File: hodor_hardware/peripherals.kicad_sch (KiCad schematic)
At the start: 59 parts, among them J2 Screw_Terminal_01x05, J3 Screw_Terminal_01x03, J5 Screw_Terminal_01x03, K1 FINDER-32.21-x000, K2 FINDER-32.21-x000, Q2 FDG1024NZ, Q3 FDG1024NZ, Q4 FDG1024NZ, Q6 BSS138DW, T4 IN2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

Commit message: Schematic finished
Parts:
- removed Q4: FDG1024NZ, Package_TO_SOT_SMD:SOT-363_SC-70-6, symbol Transistor_FET:FDG1024NZ
- added D25, D31: PMEG6010, Diode_SMD:D_SOD-128, symbol Device:D_Schottky
- added D32, D33: BCX84C15V, Diode_SMD:D_SOD-523, symbol Device:D_Zener
- added F2, F3: 1A, Diode_SMD:D_1812_4532Metric, symbol Device:Polyfuse_Small
- added J10: Screw_Terminal_01x03, TerminalBlock_Phoenix:TerminalBlock_Phoenix_PT-1,5-3-3.5-H_1x03_P3.50mm_Horizontal, symbol Connector:Screw_Terminal_01x03
- added Q10: BC847BDW1, Package_TO_SOT_SMD:SOT-363_SC-70-6, symbol Transistor_BJT:BC847BDW1
- added unit 1 of Q3
- added Q9: DMP6050SSD, Package_SO:SOIC-8_3.9x4.9mm_P1.27mm, symbol Transistor_FET:DMP6050SSD
- added R78, R80, R83, R84: 10k, Resistor_SMD:R_0402_1005Metric, symbol Device:R
- added R79, R82: 1k, Resistor_SMD:R_0402_1005Metric, symbol Device:R
- added R81, R85: 2.2k, Resistor_SMD:R_0402_1005Metric, symbol Device:R
- C3, C4, C5, C6, C7, C8: value 100n -> 100nF
- J2: footprint (none) -> TerminalBlock_Phoenix:TerminalBlock_Phoenix_PT-1,5-5-3.5-H_1x05_P3.50mm_Horizontal
- J3, J5: footprint (none) -> TerminalBlock_Phoenix:TerminalBlock_Phoenix_PT-1,5-3-3.5-H_1x03_P3.50mm_Horizontal
- T4, T5, T7, T8: now left out of the parts list
- U3, U4: footprint (none) -> Package_TO_SOT_SMD:SOT-23-6
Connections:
- net GND: now also D25.2 (A), D31.2 (A), J10.1 (Pin_1), Q10.1 (E1), Q10.4 (E2), Q3.1 (S), R80.1, R83.1
- net at D12.2 (A), R9.2: now also Q3.6 (D); no longer Q3.3 (D)
- net at D15.2 (A), R11.2: now also Q3.3 (D)
- net at R10.1, R18.1: now also Q3.5 (G)
- net at R16.1, R8.1: now also Q3.2 (G); no longer Q3.5 (G)
- new net: F3.1, Q9.5 (D2), Q9.6 (D2)
- new net: D31.1 (K), F3.2, J10.2 (Pin_2)
- new net: D25.1 (K), F2.2, J10.3 (Pin_3)
- new net: Q10.2 (B1), R79.2, R80.2
- new net: Q10.6 (C1), R81.2
- new net: D32.2 (A), Q9.2 (G1), R78.2, R81.1
- new net: Q10.3 (C2), R85.2
- new net: Q10.5 (B2), R82.2, R83.2
- new net: F2.1, Q9.7 (D1), Q9.8 (D1)
- new net: D33.2 (A), Q9.4 (G2), R84.2, R85.1
- new net OUT_CTRL_1: R79.1
- new net OUT_CTRL_2: R82.1
- new net V_{DC}: D32.1 (K), D33.1 (K), Q9.1 (S1), Q9.3 (S2), R78.1, R84.1
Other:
- note added: "2 switchable V_{DC} outputs with freewheeling diode and fuse"
- moved on the sheet: C5, C6, C7, D10, D11, D12, D13, D14, D15, D26, D27, D7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

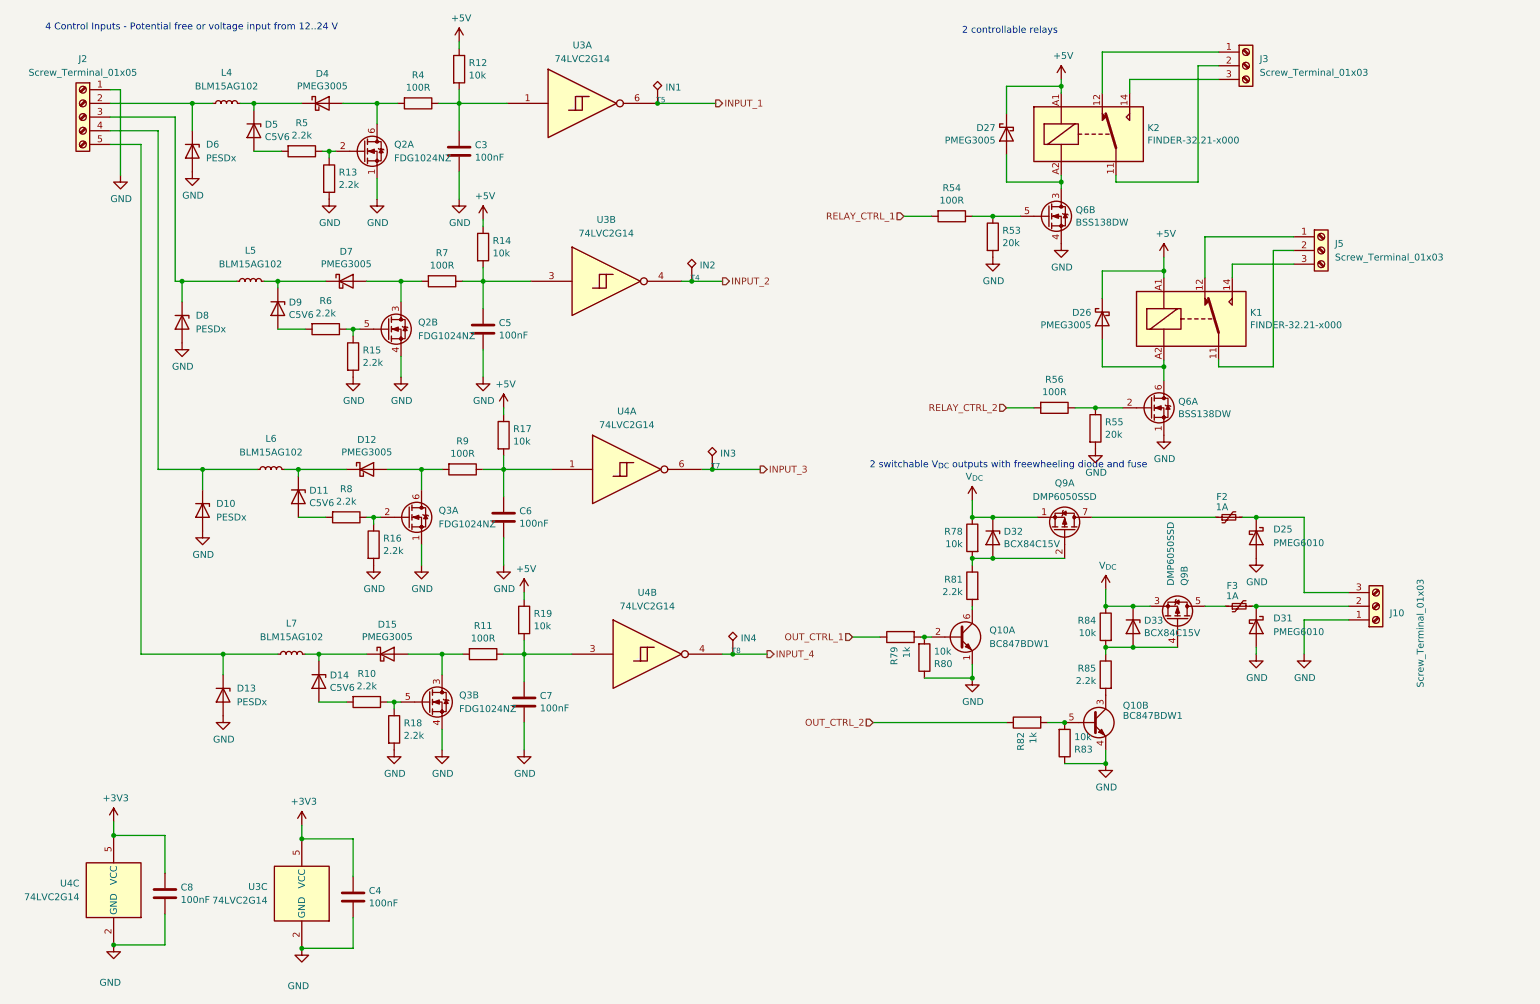
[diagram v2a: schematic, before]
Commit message: Reworked into 2 PCBs
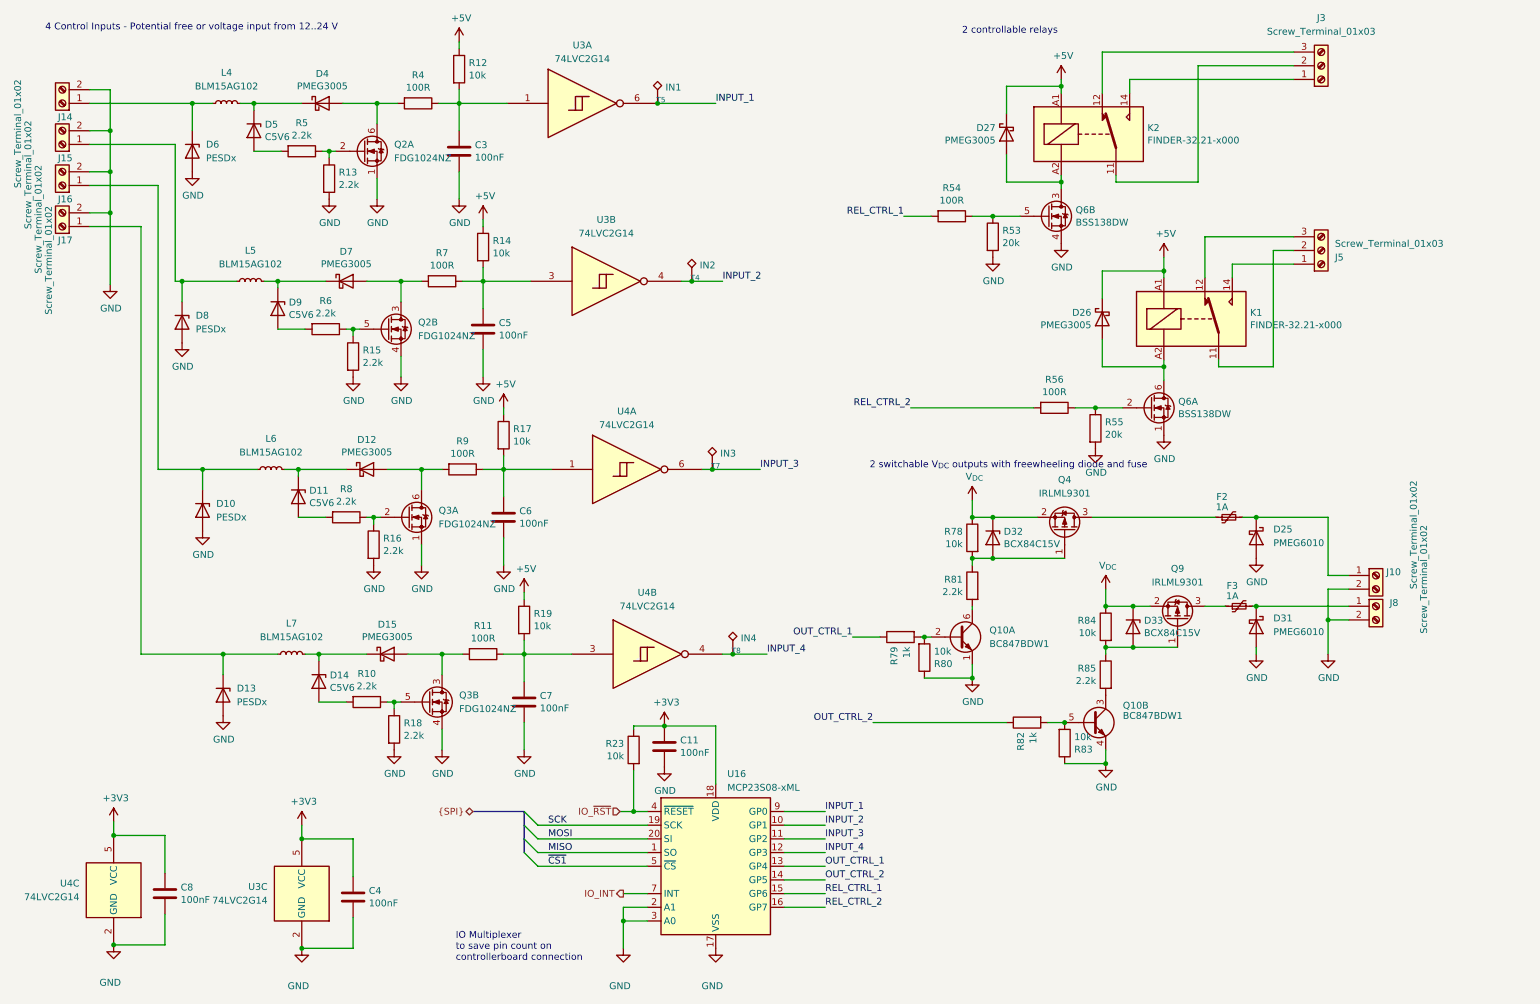
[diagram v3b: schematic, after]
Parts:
- removed J10: Screw_Terminal_01x03, TerminalBlock_Phoenix:TerminalBlock_Phoenix_PT-1,5-3-3.5-H_1x03_P3.50mm_Horizontal, symbol Connector:Screw_Terminal_01x03
- removed J2: Screw_Terminal_01x05, TerminalBlock_Phoenix:TerminalBlock_Phoenix_PT-1,5-5-3.5-H_1x05_P3.50mm_Horizontal, symbol Connector:Screw_Terminal_01x05
- removed Q9: DMP6050SSD, Package_SO:SOIC-8_3.9x4.9mm_P1.27mm, symbol Transistor_FET:DMP6050SSD
- added C11: 100nF, Capacitor_SMD:C_0402_1005Metric, symbol Device:C
- added J10, J14, J15, J16, J17, J8: Screw_Terminal_01x02, TerminalBlock_Phoenix:TerminalBlock_Phoenix_PT-1,5-2-3.5-H_1x02_P3.50mm_Horizontal, symbol Connector:Screw_Terminal_01x02
- added Q4, Q9: IRLML9301, Package_TO_SOT_SMD:SOT-23, symbol Transistor_FET:IRLML9301
- added R23: 10k, Resistor_SMD:R_0402_1005Metric, symbol Device:R
- added U16: MCP23S08-xML, Package_DFN_QFN:QFN-20-1EP_4x4mm_P0.5mm_EP2.7x2.7mm, symbol hodor_custom_parts:MCP23S08-xML
- D10, D13, D6, D8: footprint Diode_SMD:D_SOD-523 -> Diode_SMD:Nexperia_DSN1608-2_1.6x0.8mm
- D25, D31: footprint Diode_SMD:D_SOD-128 -> Diode_SMD:D_SOD-123F
- F2, F3: footprint Diode_SMD:D_1812_4532Metric -> Fuse:Fuse_1210_3225Metric
- J3, J5: footprint TerminalBlock_Phoenix:TerminalBlock_Phoenix_PT-1,5-3-3.5-H_1x03_P3.50mm_Horizontal -> TerminalBlock_Phoenix:TerminalBlock_Phoenix_MKDS-1,5-3_1x03_P5.00mm_Horizontal
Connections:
- net +3V3: now also C11.1, R23.1, U16.18 (VDD)
- net GND: now also C11.2, J10.2 (Pin_2), J14.2 (Pin_2), J15.2 (Pin_2), J16.2 (Pin_2), J17.2 (Pin_2), J8.2 (Pin_2), U16.17 (VSS), U16.2 (A1), U16.3 (A0)
- net INPUT_1: now also U16.9 (GP0)
- net INPUT_2: now also U16.10 (GP1)
- net INPUT_3: now also U16.11 (GP2)
- net INPUT_4: now also U16.12 (GP3)
- net OUT_CTRL_1: now also U16.13 (GP4)
- net OUT_CTRL_2: now also U16.14 (GP5)
- net V_{DC}: now also Q4.2 (S), Q9.2 (S)
- net at K2.12: now also J3.3 (Pin_3); no longer J3.1 (Pin_1)
- net at K2.14: now also J3.1 (Pin_1); no longer J3.3 (Pin_3)
- net at K1.12: now also J5.3 (Pin_3); no longer J5.1 (Pin_1)
- net at K1.14: now also J5.1 (Pin_1); no longer J5.3 (Pin_3)
- net at F3.1: now also Q9.3 (D)
- net at D31.1 (K), F3.2: now also J8.1 (Pin_1)
- net at D6.1 (K), L4.1: now also J14.1 (Pin_1)
- net at D8.1 (K), L5.1: now also J15.1 (Pin_1)
- net at D10.1 (K), L6.1: now also J16.1 (Pin_1)
- net at D13.1 (K), L7.1: now also J17.1 (Pin_1)
- net at D25.1 (K), F2.2: now also J10.1 (Pin_1)
- net at D32.2 (A), R78.2, R81.1: now also Q4.1 (G)
- net at F2.1: now also Q4.3 (D)
- net at D33.2 (A), R84.2, R85.1: now also Q9.1 (G)
- net RELAY_CTRL_1 renamed REL_CTRL_1
- net REL_CTRL_1: now also U16.15 (GP6)
- net RELAY_CTRL_2 renamed REL_CTRL_2
- net REL_CTRL_2: now also U16.16 (GP7)
- new net IO_INT: U16.7 (INT)
- new net IO_~{RST}: R23.2, U16.4 (~{RESET})
- new net MISO: U16.1 (SO)
- new net MOSI: U16.20 (SI)
- new net SCK: U16.19 (SCK)
- new net ~{CS1}: U16.5 (~{CS})
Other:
- note added: "IO Multiplexer to save pin count on controllerboard connection"
- moved on the sheet: J3

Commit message: Finished schematic and initial placement on PCB
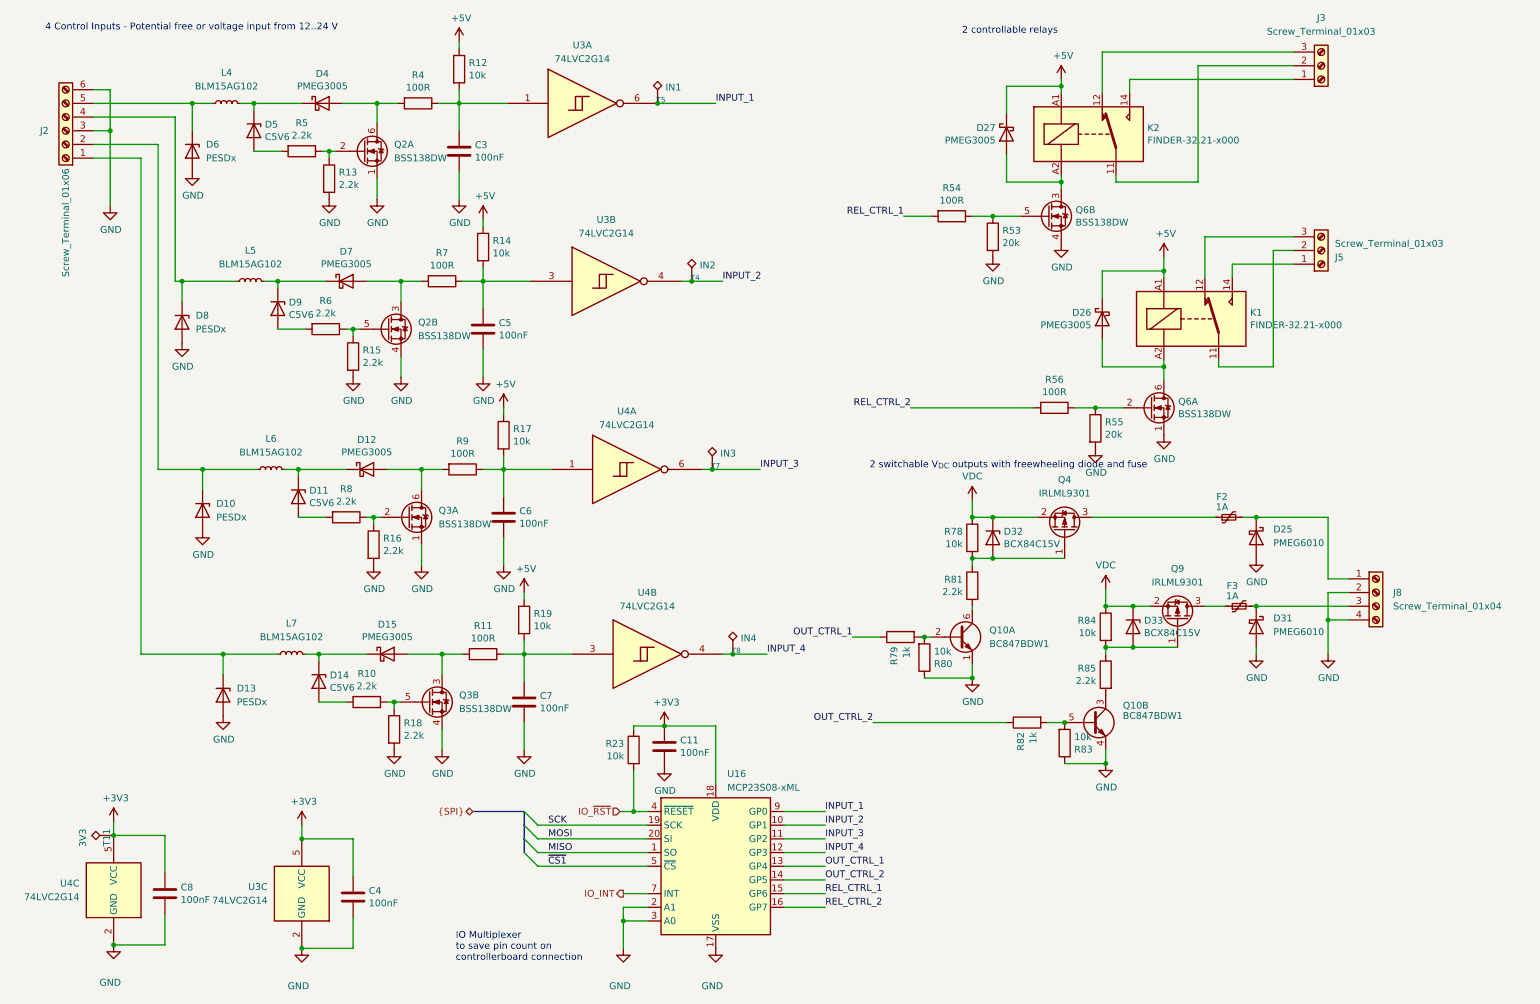
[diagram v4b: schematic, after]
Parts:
- removed J10, J14, J15, J16, J17, J8: Screw_Terminal_01x02, TerminalBlock_Phoenix:TerminalBlock_Phoenix_PT-1,5-2-3.5-H_1x02_P3.50mm_Horizontal, symbol Connector:Screw_Terminal_01x02
- added J2: Screw_Terminal_01x06, TerminalBlock_Phoenix:TerminalBlock_Phoenix_MKDS-1,5-6_1x06_P5.00mm_Horizontal, symbol Connector:Screw_Terminal_01x06
- added J8: Screw_Terminal_01x04, TerminalBlock_Phoenix:TerminalBlock_Phoenix_MKDS-1,5-4_1x04_P5.00mm_Horizontal, symbol Connector:Screw_Terminal_01x04
- added T11: 3V3, TestPoint:TestPoint_Pad_D1.0mm, symbol Connector:TestPoint_Alt
- Q2, Q3: value FDG1024NZ -> BSS138DW
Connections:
- net +3V3: now also T11.1
- net GND: now also J2.3 (Pin_3), J2.6 (Pin_6), J8.2 (Pin_2), J8.4 (Pin_4)
- net at D10.1 (K), L6.1: now also J2.2 (Pin_2)
- net at D31.1 (K), F3.2: now also J8.3 (Pin_3)
- net at D25.1 (K), F2.2: now also J8.1 (Pin_1)
- net at D8.1 (K), L5.1: now also J2.4 (Pin_4)
- net at D6.1 (K), L4.1: now also J2.5 (Pin_5)
- net at D13.1 (K), L7.1: now also J2.1 (Pin_1)
- net V_{DC} renamed VDC

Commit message: Initialized SW project
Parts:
- D10, D13, D6, D8: footprint Diode_SMD:Nexperia_DSN1608-2_1.6x0.8mm -> Diode_SMD:D_SOD-523
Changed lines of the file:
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@@
 			)
 		)
-		(property "Footprint" "Diode_SMD:Nexperia_DSN1608-2_1.6x0.8mm"
+		(property "Footprint" "Diode_SMD:D_SOD-523"
 			(at 41.91 41.275 0)
 			(effects
@@
 			)
 		)
-		(property "Footprint" "Diode_SMD:Nexperia_DSN1608-2_1.6x0.8mm"
+		(property "Footprint" "Diode_SMD:D_SOD-523"
 			(at 40.005 73.025 0)
 			(effects
@@
 			)
 		)
-		(property "Datasheet" "https://assets.nexperia.com/documents/data-sheet/PTVS26VZ1USK.pdf"
+		(property "Datasheet" ""
 			(at 44.45 73.025 0)
 			(effects
@@
 			)
 		)
-		(property "Description" "26V, 1850W TVS unidirectional diode, DSN1608-2"
+		(property "Description" ""
 			(at 44.45 73.025 0)
 			(effects
@@
 			)
 		)
-		(property "Footprint" "Diode_SMD:Nexperia_DSN1608-2_1.6x0.8mm"
+		(property "Footprint" "Diode_SMD:D_SOD-523"
 			(at 47.625 142.24 0)
 			(effects
@@
 			)
 		)
-		(property "Datasheet" "https://assets.nexperia.com/documents/data-sheet/PTVS26VZ1USK.pdf"
+		(property "Datasheet" ""
 			(at 52.07 142.24 0)
 			(effects
@@
 			)
 		)
-		(property "Description" "26V, 1850W TVS unidirectional diode, DSN1608-2"
+		(property "Description" ""
 			(at 52.07 142.24 0)
 			(effects
@@
 			)
 		)
-		(property "Footprint" "Diode_SMD:Nexperia_DSN1608-2_1.6x0.8mm"
+		(property "Footprint" "Diode_SMD:D_SOD-523"
 			(at 43.815 107.95 0)
 			(effects
@@
 			)
 		)
-		(property "Datasheet" "https://assets.nexperia.com/documents/data-sheet/PTVS26VZ1USK.pdf"
+		(property "Datasheet" ""
 			(at 48.26 107.95 0)
 			(effects
@@
 			)
 		)
-		(property "Description" "26V, 1850W TVS unidirectional diode, DSN1608-2"
+		(property "Description" ""
 			(at 48.26 107.95 0)
 			(effects
